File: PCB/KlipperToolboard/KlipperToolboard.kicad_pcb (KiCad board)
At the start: 2 copper layers, 47.9 x 34.9 mm, 51 parts, among them J1 Endstop, J2 Servo, J3 HeaterThermistor, J4 PartFan, J5 HeaterFan, J6 Heater, J7 Conn_02x03_Counter_Clockwise, J8 PWRUART, J9 Stepper, Q1 AO3400A, Q2 AO3400A, Q3 WSF3085, U1 ATmega168A-AU, U2 TMC2209-LA, Y1 16Mhz

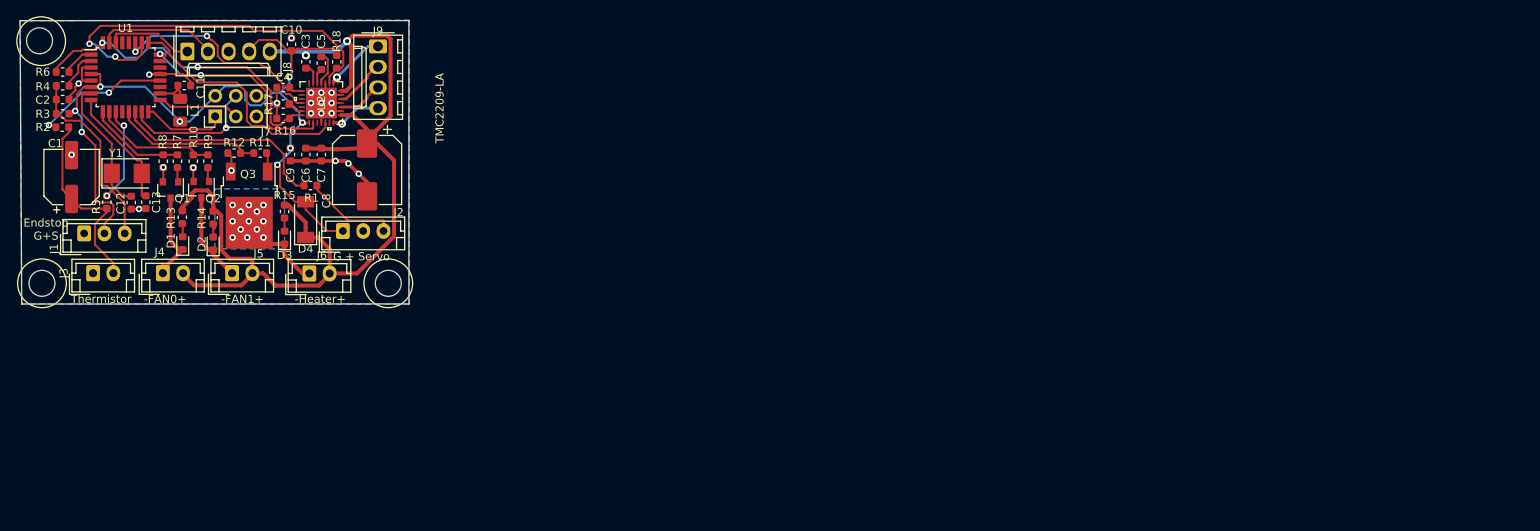
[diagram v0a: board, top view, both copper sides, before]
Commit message: Changed to STM32
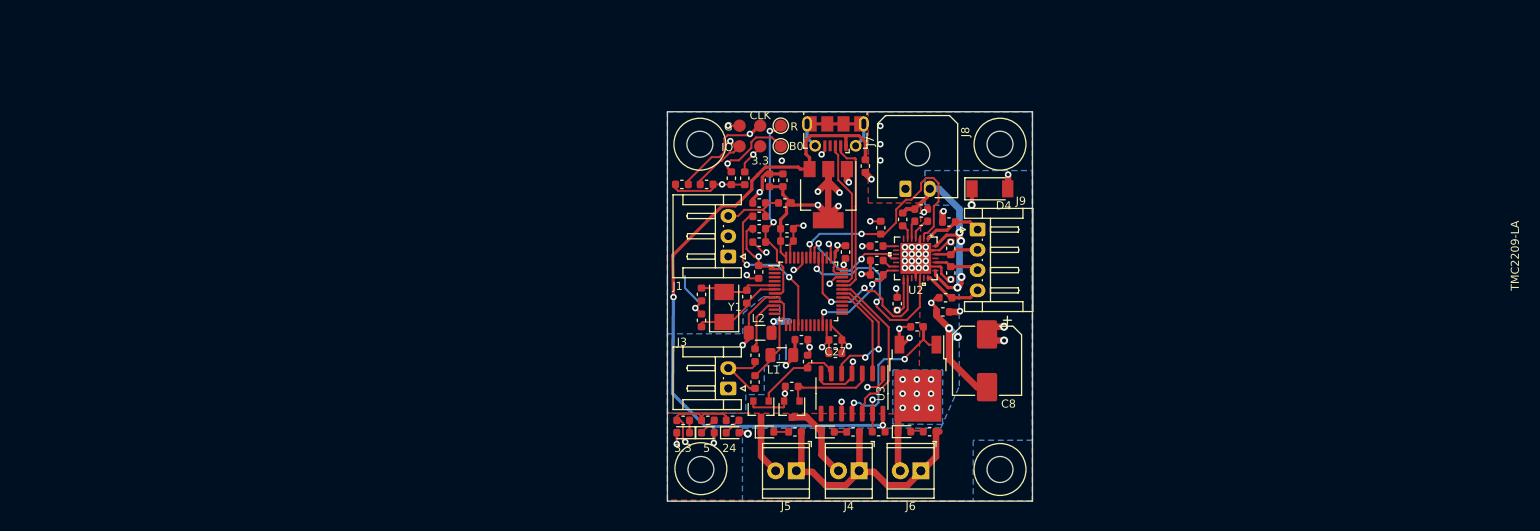
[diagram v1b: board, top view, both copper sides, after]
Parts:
- removed R6: 1K, Resistor_SMD:R_0603_1608Metric
- removed R7: 10R, Resistor_SMD:R_0603_1608Metric
- added C14: 0.1uF, Capacitor_SMD:C_0603_1608Metric, F.Cu at (209.0, 138.9)
- added C15: 0.1uF, Capacitor_SMD:C_0603_1608Metric, F.Cu at (207.4, 106.2)
- added C16: 0.1uF, Capacitor_SMD:C_0603_1608Metric, F.Cu at (195.6, 108.0)
- added C17: 0.1uF, Capacitor_SMD:C_0603_1608Metric, F.Cu at (205.0, 116.8)
- added C18: 0.1uF, Capacitor_SMD:C_0603_1608Metric, F.Cu at (194.2, 119.2)
- added C19: 0.1uF, Capacitor_SMD:C_0603_1608Metric, F.Cu at (194.3, 115.6)
- added C20: 470p, Capacitor_SMD:C_0603_1608Metric, F.Cu at (217.9, 119.4)
- added C21: 470p, Capacitor_SMD:C_0603_1608Metric, F.Cu at (217.3, 122.4)
- added C22: 470p, Capacitor_SMD:C_0603_1608Metric, F.Cu at (217.9, 116.3)
- added C23: 470p, Capacitor_SMD:C_0603_1608Metric, F.Cu at (217.7, 113.1)
- added C24: 0.1uF, Capacitor_SMD:C_0603_1608Metric, F.Cu at (192.5, 107.7)
- added C25: 22uF, Capacitor_SMD:C_0603_1608Metric, F.Cu at (197.2, 108.0)
- added C26: 0.1uF, Capacitor_SMD:C_0603_1608Metric, F.Cu at (197.7, 113.9)
- added C27: 4.7uF, Capacitor_SMD:C_0603_1608Metric, F.Cu at (203.7, 127.6)
- added D6: LED, LED_SMD:LED_0603_1608Metric, F.Cu at (191.0, 139.1)
- added D7: LED, LED_SMD:LED_0603_1608Metric, F.Cu at (188.0, 139.1)
- added D8: LED, LED_SMD:LED_0603_1608Metric, F.Cu at (184.9, 139.1)
- added L2: 22uH, Inductor_SMD:L_1206_3216Metric, F.Cu at (194.4, 126.8)
- added R19: 2.2k, Resistor_SMD:R_0603_1608Metric, F.Cu at (188.0, 137.5)
- added R20: 2.2k, Resistor_SMD:R_0603_1608Metric, F.Cu at (184.9, 137.5)
- added R21: 10k, Resistor_SMD:R_0603_1608Metric, F.Cu at (184.8, 108.5)
- added R22: 10k, Resistor_SMD:R_0603_1608Metric, F.Cu at (187.8, 108.5)
- added R23: 10k, Resistor_SMD:R_0603_1608Metric, F.Cu at (190.9, 107.7)
- added TP1: BOOT0, TestPoint:TestPoint_Pad_D1.5mm, F.Cu at (197.0, 103.8)
- added TP2: NRST, TestPoint:TestPoint_Pad_D1.5mm, F.Cu at (197.0, 101.2)
- added U3: 74HC125, Package_SO:SOIC-14_3.9x8.7mm_P1.27mm, F.Cu at (205.7, 134.2)
- added U4: AMS1117-3.3, Package_TO_SOT_SMD:SOT-223-3_TabPin2, F.Cu at (202.8, 109.7)
- C1: value 10uF/35V -> 4.7uF; footprint Capacitor_SMD:CP_Elec_6.3x5.8 -> Capacitor_SMD:C_0603_1608Metric
- C3: value 100nf/50V -> 100nF/50V
- D4: value D_Schottky -> B5819W
- J1: footprint Connector_JST:JST_EH_B3B-EH-A_1x03_P2.50mm_Vertical -> Connector_JST:JST_EH_S3B-EH_1x03_P2.50mm_Horizontal
- J2: value Servo -> Conn_01x04; footprint Connector_JST:JST_EH_B3B-EH-A_1x03_P2.50mm_Vertical -> KlipperToolboard:Testpad 02x02 2.54
- J3: footprint Connector_JST:JST_EH_B2B-EH-A_1x02_P2.50mm_Vertical -> Connector_JST:JST_EH_S2B-EH_1x02_P2.50mm_Horizontal
- J4, J5, J6: footprint Connector_JST:JST_EH_B2B-EH-A_1x02_P2.50mm_Vertical -> TerminalBlock_TE-Connectivity:TerminalBlock_TE_282834-2_1x02_P2.54mm_Horizontal
- J7: value Conn_02x03_Counter_Clockwise -> USB_B_Micro; footprint Connector_PinHeader_2.54mm:PinHeader_2x03_P2.54mm_Vertical -> Connector_USB:USB_Micro-B_Molex-105017-0001
- J8: value PWRUART -> Conn_01x02; footprint Connector_Molex:Molex_KK-254_AE-6410-05A_1x05_P2.54mm_Vertical -> Connector_Molex:Molex_Micro-Fit_3.0_43650-0200_1x02_P3.00mm_Horizontal
- J9: footprint Connector_Molex:Molex_KK-254_AE-6410-04A_1x04_P2.54mm_Vertical -> Connector_JST:JST_EH_S4B-EH_1x04_P2.50mm_Horizontal
- L1: value 10uH -> 22uH
- R1: value 100R -> 4.7k
- R10, R12, R8: value 100k -> 10k
- R11: value 10R -> 6.8k
- R2: value 4.7K -> 4.7k 1%
- R5: value 100R -> 10k
- R9: value 10R -> 1M
- U1: value ATmega168A-AU -> STM32F103C8T6; footprint Package_QFP:TQFP-32_7x7mm_P0.8mm -> Package_QFP:LQFP-48_7x7mm_P0.5mm
- Y1: value 16Mhz -> 8Mhz
- moved R2 91.0 mm to (193.8, 132.8), turned to 90 degrees
- moved J8 90.1 mm to (212.3, 109.0)
- moved R3 89.7 mm to (197.5, 110.7)
- moved J4 89.2 mm to (206.6, 143.8), turned to 180 degrees
- moved C1 88.5 mm to (197.7, 115.4), turned to 0 degrees
- moved U1 88.2 mm to (200.4, 121.7)
- moved R4 87.4 mm to (194.3, 112.4), turned to 0 degrees
- moved R12 86.9 mm to (213.8, 126.0)
- moved R13 86.8 mm to (205.9, 139.0), turned to 180 degrees
- moved C2 86.8 mm to (194.3, 110.7), turned to 0 degrees
- moved Q3 85.1 mm to (213.9, 132.4)
- moved D4 84.4 mm to (222.8, 109.0), turned to 0 degrees
- moved R15 84.0 mm to (215.3, 138.9), turned to 180 degrees
- moved D1 82.9 mm to (202.8, 139.0), turned to 0 degrees
- moved R8 82.3 mm to (198.3, 133.4), turned to 0 degrees
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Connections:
- C1 pad 1: Net-(C1-Pad1) -> +3V3
- C10 pad 1: VCC -> +3V3
- C11 pad 2: Net-(C11-Pad2) -> +3V3
- C9 pad 2: VCC -> +3V3
- D4 pad 2: VCC -> +3V3
- J1 pad 2: VCC -> +3V3
- J2 pad 1: VCC -> +3V3
- J2 pad 2: GND -> SWDIO
- J2 pad 3: Net-(J2-Pad3) -> SWCLK
- J3 pad 1: GND -> GNDA
- J3 pad 2: Net-(C1-Pad1) -> Net-(J3-Pad2)
- J4 pad 1: Net-(D1-Pad1) -> ST_VS
- J4 pad 2: ST_VS -> Net-(D1-Pad1)
- J5 pad 1: Net-(D2-Pad1) -> ST_VS
- J5 pad 2: ST_VS -> Net-(D2-Pad1)
- J6 pad 1: Net-(D3-Pad1) -> ST_VS
- J6 pad 2: ST_VS -> Net-(D3-Pad1)
- J7 pad 1: MISO -> VBUS
- J7 pad 2: VCC -> USBD-
- J7 pad 3: SCK -> USBD+
- J7 pad 4: MOSI -> (no net)
- J7 pad 5: (no net) -> GND
- J7 pad 6: GND -> Net-(J7-Pad6)
- J8 pad 1: RX -> GND
- J8 pad 2: TX -> ST_VS
- L1 pad 1: VCC -> +3V3
- L1 pad 2: Net-(C11-Pad2) -> AREF
- Q1 pad 1: Net-(Q1-Pad1) -> PARTFAN_MOS
- Q2 pad 1: Net-(Q2-Pad1) -> HEATERFAN_MOS
- Q3 pad 1: Net-(Q3-Pad1) -> HEATER_MOS
- R1 pad 1: SERVO -> +3V3
- R1 pad 2: Net-(J2-Pad3) -> Net-(C19-Pad2)
- R10 pad 2: HEATERFAN -> HEATERFAN_MOS
- R11 pad 1: Net-(Q3-Pad1) -> Net-(D6-Pad1)
- R11 pad 2: HEATER -> GND
- R12 pad 2: HEATER -> HEATER_MOS
- R18 pad 1: VCC -> +3V3
- R2 pad 1: Net-(C1-Pad1) -> Net-(J3-Pad2)
- R3 pad 1: VCC -> +3V3
- R5 pad 2: Net-(C1-Pad1) -> Net-(J3-Pad2)
- R8 pad 2: PARTFAN -> PARTFAN_MOS
- R9 pad 1: Net-(Q2-Pad1) -> Net-(C12-Pad2)
- R9 pad 2: HEATERFAN -> Net-(C13-Pad2)
- U1 pad 1: Net-(R6-Pad2) -> +3V3
- U1 pad 10: HEATERFAN -> THERM
- U1 pad 11: THERM -> (no net)
- U1 pad 13: HEATER -> (no net)
- U1 pad 14: SERVO -> (no net)
- U1 pad 15: MOSI -> (no net)
- U1 pad 16: MISO -> ENDSTOP
- U1 pad 17: SCK -> (no net)
- U1 pad 18: Net-(C11-Pad2) -> (no net)
- U1 pad 2: ENDSTOP -> (no net)
- U1 pad 20: AREF -> (no net)
- U1 pad 21: GND -> (no net)
- U1 pad 22: (no net) -> ST_UART
- U1 pad 23: (no net) -> GND
- U1 pad 24: ST_STEP -> +3V3
- U1 pad 25: ST_DIR -> (no net)
- U1 pad 26: ST_EN -> (no net)
- U1 pad 27: ST_DIAG -> (no net)
- U1 pad 29: (no net) -> PARTFAN
- U1 pad 3: GND -> (no net)
- U1 pad 30: RX -> HEATERFAN
- U1 pad 31: TX -> HEATER
- U1 pad 32: ST_UART -> USBD-
- U1 pad 4: VCC -> (no net)
- U1 pad 5: GND -> Net-(C13-Pad2)
- U1 pad 6: VCC -> Net-(C12-Pad2)
- U1 pad 7: Net-(C12-Pad2) -> Net-(C19-Pad2)
- U1 pad 8: Net-(C13-Pad2) -> GNDA
- U1 pad 9: PARTFAN -> AREF
- U2 pad 15: VCC -> +3V3
- U2 pad 25: GND -> (no net)
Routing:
- net VCC: track 100.9 -> 0.00 mm, vias 8 -> 0
- net GND: track 45.2 -> 141.2 mm, vias 21 -> 52
- net VBUS: track 0.00 -> 88.8 mm, vias 0 -> 3
- net +3V3: track 0.00 -> 73.8 mm, vias 0 -> 13
- net ST_VS: track 127.9 -> 74.2 mm, vias 2 -> 9
- net SWCLK: track 0.00 -> 34.3 mm, vias 0 -> 2
- net SWDIO: track 0.00 -> 34.0 mm, vias 0 -> 2
- net Net-(R23-Pad2): track 0.00 -> 31.1 mm, vias 0 -> 2
- net ST_UART: track 40.1 -> 13.3 mm
- net SERVO: track 26.6 -> 0.00 mm
- net Net-(C19-Pad2): track 0.00 -> 24.4 mm, vias 0 -> 2
- net Net-(C1-Pad1): track 24.2 -> 0.00 mm
- net HEATER_MOS: track 0.00 -> 20.9 mm, vias 0 -> 2
- net USBD-: track 0.00 -> 19.9 mm
- net USBD+: track 0.00 -> 18.6 mm
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- added copper zone on In1.Cu, net +3V3
- added copper zone on F.Cu, net GND
- added copper zone on In2.Cu, net GND
- added copper zone on B.Cu, net GNDA
- added copper zone on B.Cu, net ST_VS
- added copper zone on In1.Cu, net ST_VS
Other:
- board size 47.9 x 34.9 mm -> 45 x 48 mm
- copper layers 2 -> 4
- net class StepperPin added: clearance 0.2, trace_width 0.32, via_dia 0.8, via_drill 0.4
- board text added: "24"
- board text added: "3.3"
- board text added: "5"
- board text added: "B0"
- board text added: "CLK"
- board text added: "G"
- board text added: "IO"
- board text added: "R"
- board text removed: "-FAN0+"
- board text removed: "-FAN1+"
- board text removed: "-Heater+"
- board text removed: "Endstop G+S"
- board text removed: "G + Servo"
- board text removed: "Thermistor"

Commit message: Change to STM32 and CAN Bus
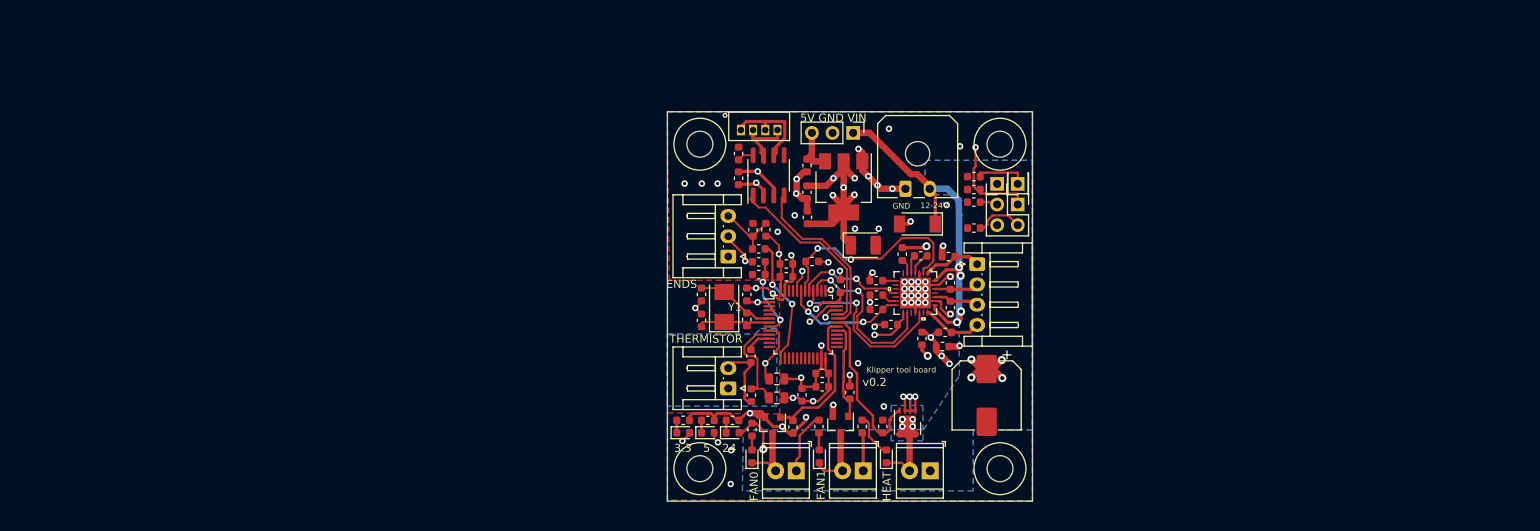
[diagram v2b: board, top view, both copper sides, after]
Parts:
- removed Q3: WSF3085, Package_TO_SOT_SMD:TO-252-2
- removed U1: STM32F103C8T6, Package_QFP:LQFP-48_7x7mm_P0.5mm
- removed U3: 74HC125, Package_SO:SOIC-14_3.9x8.7mm_P1.27mm
- added C28: 0.1uF, Capacitor_SMD:C_0603_1608Metric, F.Cu at (191.8, 107.7)
- added J10: Conn_01x04_Male, KlipperToolboard:JST-ZH-THRx4, F.Cu at (194.3, 101.8)
- added Q4: AON7418, KlipperToolboard:DFN-8-1EP_3x3mm_P0.65mm_EP1.7x2.05mm, F.Cu at (212.6, 137.8)
- added R6: 10k, Resistor_SMD:R_0603_1608Metric, F.Cu at (191.8, 104.6)
- added U5: STM32F042C6T6, Package_QFP:LQFP-48_7x7mm_P0.5mm, F.Cu at (199.7, 125.7)
- added U6: SN65HVD230, Package_SO:SOIC-8_3.9x4.9mm_P1.27mm, F.Cu at (195.5, 107.3)
- C14: value 0.1uF -> 100uF/50V; footprint Capacitor_SMD:C_0603_1608Metric -> Capacitor_Tantalum_SMD:CP_EIA-3528-12_Kemet-T
- J2: footprint KlipperToolboard:Testpad 02x02 2.54 -> Connector_PinHeader_2.54mm:PinHeader_2x02_P2.54mm_Vertical
- J7: value USB_B_Micro -> Conn_01x03; footprint Connector_USB:USB_Micro-B_Molex-105017-0001 -> Connector_PinHeader_2.54mm:PinHeader_1x03_P2.54mm_Vertical
- L1, L2: footprint Inductor_SMD:L_1206_3216Metric -> Inductor_SMD:L_0805_2012Metric
- TP1, TP2: footprint TestPoint:TestPoint_Pad_D1.5mm -> Connector_PinHeader_2.54mm:PinHeader_1x01_P2.54mm_Vertical
- moved R21 36.1 mm to (220.8, 110.6)
- moved R22 33.4 mm to (220.8, 113.8), turned to 0 degrees
- moved J2 31.0 mm to (226.2, 110.9), turned to 270 degrees
- moved R23 29.9 mm to (220.8, 107.5), turned to 0 degrees
- moved TP1 29.6 mm to (226.2, 108.4), turned to 90 degrees
- moved C24 28.3 mm to (220.8, 109.1), turned to 180 degrees
- moved TP2 27.6 mm to (223.6, 108.4), turned to 90 degrees
- moved C14 23.1 mm to (207.1, 116.0), turned to 0 degrees
- moved C7 16.0 mm to (214.4, 127.5), turned to 90 degrees
- moved R12 13.0 mm to (209.6, 138.3), turned to 270 degrees
- moved D4 9.93 mm to (213.8, 113.3), turned to 180 degrees
- moved C26 9.50 mm to (192.8, 122.0), turned to 90 degrees
- moved R18 9.43 mm to (200.8, 118.0), turned to 180 degrees
- moved R15 8.34 mm to (207.0, 138.3), turned to 90 degrees
- moved R10 8.25 mm to (198.5, 138.4), turned to 90 degrees
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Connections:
- C14 pad 1: VBUS -> +3V3
- C15 pad 2: VBUS -> +5V
- D7 pad 2: VBUS -> +5V
- J7 pad 1: VBUS -> ST_VS
- J7 pad 2: USBD- -> GND
- J7 pad 3: USBD+ -> +5V
- Q1 pad 1: PARTFAN_MOS -> PARTFAN
- Q2 pad 1: HEATERFAN_MOS -> HEATERFAN
- R10 pad 2: HEATERFAN_MOS -> HEATERFAN
- R12 pad 2: HEATER_MOS -> HEATER
- R8 pad 2: PARTFAN_MOS -> PARTFAN
- U4 pad 3: VBUS -> +5V
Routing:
- net VBUS: track 88.8 -> 0.00 mm, vias 3 -> 0
- net +5V: track 0.00 -> 50.3 mm, vias 0 -> 1
- net GND: track 141.2 -> 113.8 mm, vias 52 -> 62
- net Net-(C19-Pad2): track 24.4 -> 51.1 mm
- net CANTX: track 0.00 -> 22.6 mm
- net CANRX: track 0.00 -> 21.4 mm
- net HEATER_MOS: track 20.9 -> 0.00 mm, vias 2 -> 0
- net USBD-: track 19.9 -> 0.00 mm
- net USBD+: track 18.6 -> 0.00 mm
- net +3V3: track 73.8 -> 87.6 mm, vias 13 -> 17
- net Net-(R23-Pad2): track 31.1 -> 44.3 mm, vias 2 -> 1
- net Net-(J7-Pad6): track 12.6 -> 0.00 mm
- net Net-(J10-Pad1): track 0.00 -> 11.8 mm
- net HEATERFAN_MOS: track 11.3 -> 0.00 mm
- net PARTFAN_MOS: track 11.1 -> 0.00 mm
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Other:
- outline, holes or cut-outs redrawn
- board text added: "12-24V"
- board text added: "5V GND VIN"
- board text added: "ENDS"
- board text added: "FAN0"
- board text added: "FAN1"
- board text added: "GND"
- board text added: "HEAT"
- board text added: "Klipper tool board"
- board text added: "THERMISTOR"
- board text added: "v0.2"
- board text removed: "B0"
- board text removed: "CLK"
- board text removed: "G"
- board text removed: "IO"
- board text removed: "R"
